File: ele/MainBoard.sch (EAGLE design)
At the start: 120 parts, among them IC1 MCP23017SP, IC2 74HC595D, IC3 74HC595D, X1 POWER_IN, X2 POWER_OUT

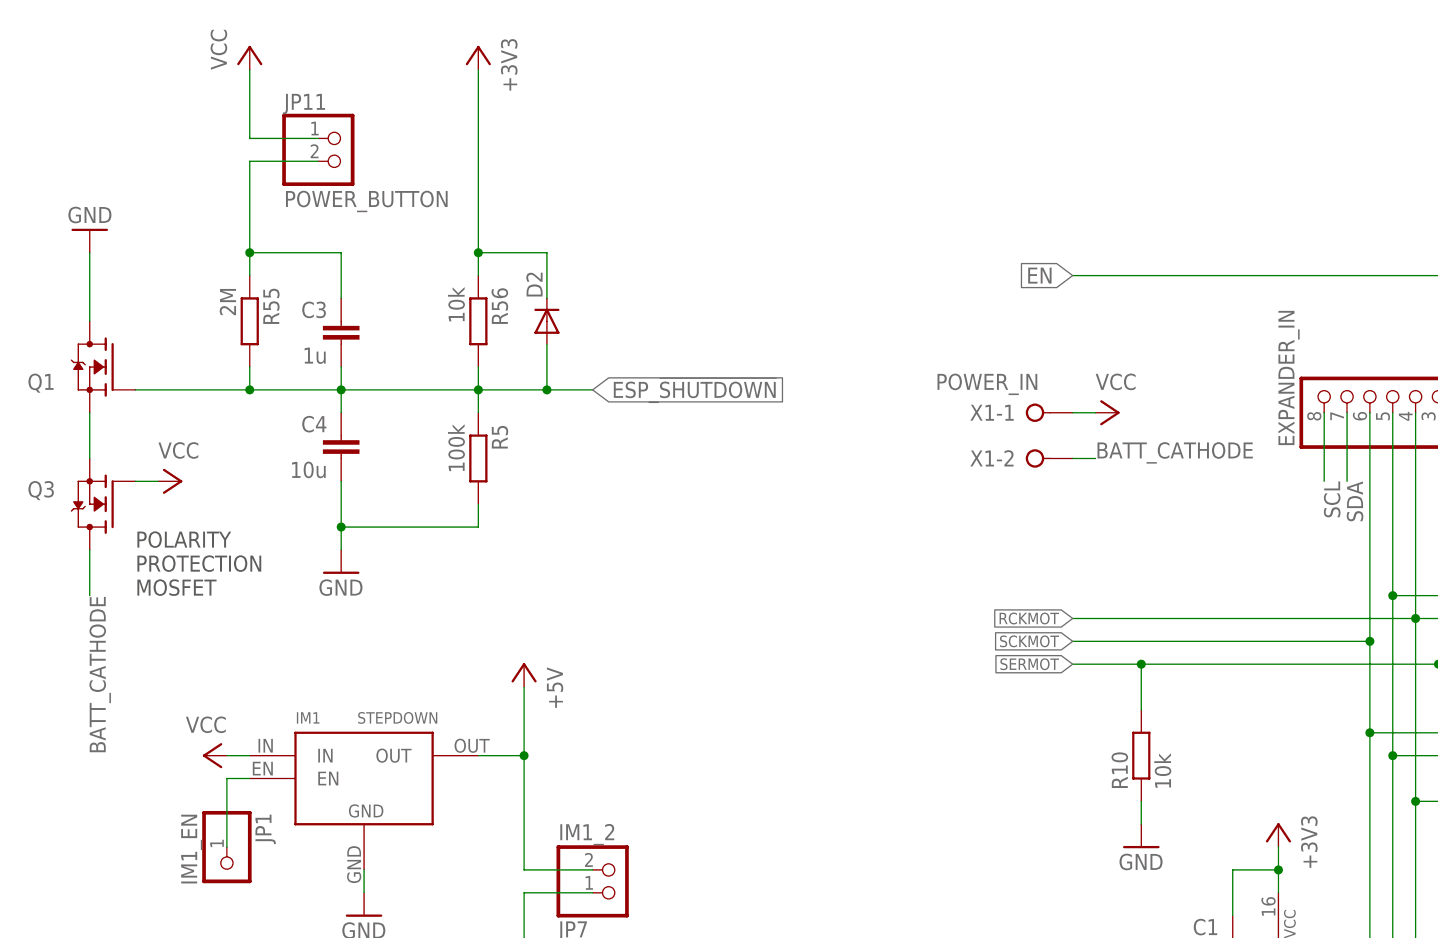
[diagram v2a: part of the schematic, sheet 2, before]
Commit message: ele: move power switch from GND to VCC (schematic only)
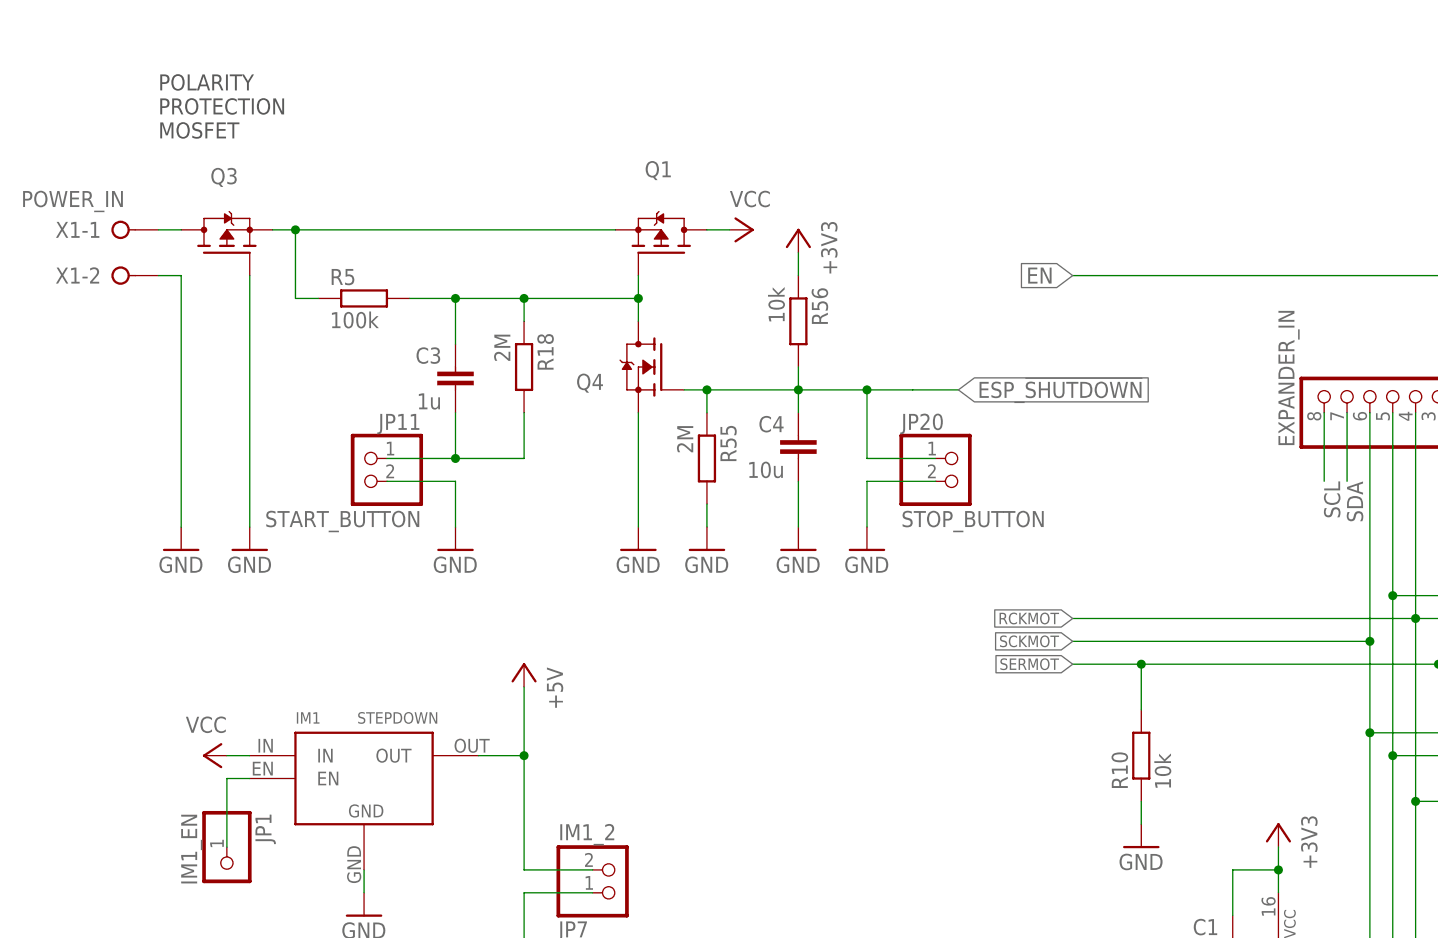
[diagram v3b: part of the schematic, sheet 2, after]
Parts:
- removed D2: (no value), diode:DIODE-SOD123
- added JP20: STOP_BUTTON, pinhead:PINHD-1X2
- added Q4: (no value), transistors:N-MOSFET-TO92
- added R18: 2M, rcl_upravena:R-EU_0204/2V
- JP11: value POWER_BUTTON -> START_BUTTON
- Q1, Q3: device transistors:N-MOSFET-TO220V -> transistors:P-MOSFET-TO220V
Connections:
- removed net BATT_CATHODE: Q3.D, X1-2.KL
- removed net BATT_CATHODE2: Q1.S, Q3.S
- removed net N$19: C3.1, JP11.2, R55.1
- new net BAT: Q3.D, X1-1.KL
- new net BAT_PROT: Q1.S, Q3.S, R5.1
- new net N$1: C3.1, Q1.G, Q4.D, R18.1, R5.2
- new net N$6: C3.2, JP11.1, R18.2
- net +3V3: no longer D2.C
- net ESP_!SHUTDOWN: now also JP20.1, Q4.G, R55.1; no longer C3.2, D2.A, Q1.G, R5.1, R55.2
- net GND: now also JP11.2, JP20.2, Q3.G, Q4.S, R55.2, X1-2.KL; no longer Q1.D, R5.2
- net VCC: now also Q1.D; no longer JP11.1, Q3.G, X1-1.KL
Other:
- moved on the sheet: C3, C4, JP11, Q1, Q3, R5, R55, R56, X1-1, X1-2

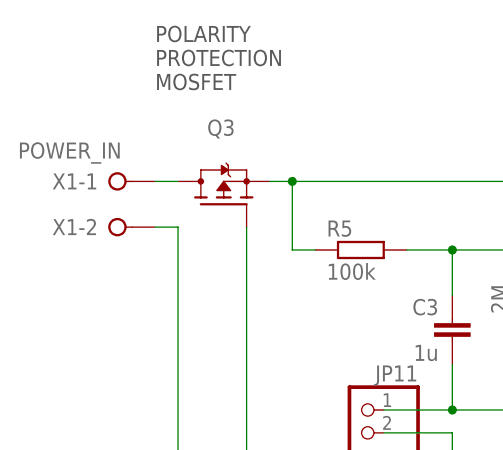
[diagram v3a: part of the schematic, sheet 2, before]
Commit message: ele: Fix layout on left side (motor drivers)
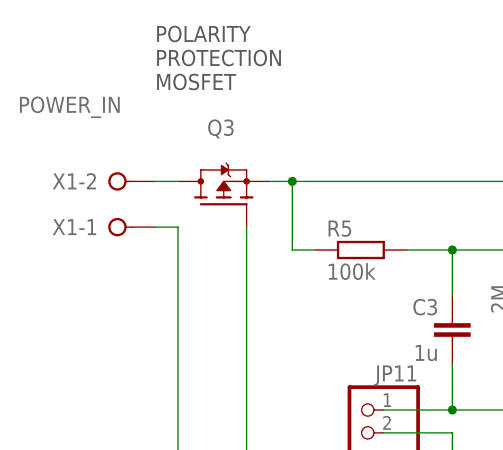
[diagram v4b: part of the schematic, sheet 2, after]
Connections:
- net BAT: now also X1-2.KL; no longer X1-1.KL
- net GND: now also X1-1.KL; no longer X1-2.KL
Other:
- moved on the sheet: X1-1, X1-2

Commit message: ele: MainBoard - join the start/stop pinheads
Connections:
- net N$1 renamed START_GATE
- net N$6 renamed START_BUTTON
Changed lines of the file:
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@@
 <?xml version="1.0" encoding="utf-8"?>
 <!DOCTYPE eagle SYSTEM "eagle.dtd">
-<eagle version="9.0.1">
+<eagle version="9.0.0">
 <drawing>
 <settings>
@@
 </segment>
 </net>
-<net name="N$1" class="0">
+<net name="START_GATE" class="0">
 <segment>
 <pinref part="R5" gate="G$1" pin="2"/>
@@
 </segment>
 </net>
-<net name="N$6" class="0">
+<net name="START_BUTTON" class="0">
 <segment>
 <pinref part="R18" gate="G$1" pin="2"/>

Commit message: ele: Added PIEZO to MainBoard.
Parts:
- added U$1: PIEZO, piezo:PIEZO
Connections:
- net ENC7A: now also U$1.+
- net ENC7B_: now also U$1.-
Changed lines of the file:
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@@
 <?xml version="1.0" encoding="utf-8"?>
 <!DOCTYPE eagle SYSTEM "eagle.dtd">
-<eagle version="9.0.0">
+<eagle version="9.0.1">
 <drawing>
 <settings>
@@
 <part name="JP20" library="pinhead" deviceset="PINHD-1X2" device="" value="STOP_BUTTON"/>
 <part name="GND52" library="supply1" library_urn="urn:adsk.eagle:library:371" deviceset="GND" device=""/>
+<part name="U$1" library="piezo" deviceset="PIEZO" device=""/>
 </parts>
 <sheets>
@@
 <instance part="GND14" gate="1" x="25.4" y="91.44"/>
 <instance part="P+27" gate="1" x="48.26" y="124.46"/>
+<instance part="U$1" gate="G$1" x="185.42" y="193.04" rot="R180"/>
 </instances>
 <busses>
@@
 <label x="205.74" y="187.96" size="1.778" layer="95" rot="R180"/>
 <pinref part="RN5" gate="B" pin="1"/>
-<wire x1="223.52" y1="187.96" x2="205.74" y2="187.96" width="0.1524" layer="91"/>
+<wire x1="223.52" y1="187.96" x2="190.5" y2="187.96" width="0.1524" layer="91"/>
+<pinref part="U$1" gate="G$1" pin="+"/>
 </segment>
 <segment>
@@
 <segment>
 <pinref part="RN5" gate="A" pin="2"/>
-<wire x1="248.92" y1="190.5" x2="233.68" y2="190.5" width="0.1524" layer="91"/>
+<wire x1="248.92" y1="190.5" x2="236.22" y2="190.5" width="0.1524" layer="91"/>
 <pinref part="IM6" gate="G$1" pin="IO33"/>
 <label x="238.76" y="190.5" size="1.778" layer="95"/>
+<wire x1="236.22" y1="190.5" x2="233.68" y2="190.5" width="0.1524" layer="91"/>
+<wire x1="236.22" y1="190.5" x2="236.22" y2="195.58" width="0.1524" layer="91"/>
+<wire x1="236.22" y1="195.58" x2="193.04" y2="195.58" width="0.1524" layer="91"/>
+<junction x="236.22" y="190.5"/>
+<pinref part="U$1" gate="G$1" pin="-"/>
+<wire x1="193.04" y1="195.58" x2="193.04" y2="190.5" width="0.1524" layer="91"/>
+<wire x1="193.04" y1="190.5" x2="190.5" y2="190.5" width="0.1524" layer="91"/>
 </segment>
 </net>

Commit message: ele: Modified tNames layer on the PCB design.
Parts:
- renumbered U$1 to PIEZO
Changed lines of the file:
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@@
 <part name="JP20" library="pinhead" deviceset="PINHD-1X2" device="" value="STOP_BUTTON"/>
 <part name="GND52" library="supply1" library_urn="urn:adsk.eagle:library:371" deviceset="GND" device=""/>
-<part name="U$1" library="piezo" deviceset="PIEZO" device=""/>
+<part name="PIEZO" library="piezo" deviceset="PIEZO" device=""/>
 </parts>
 <sheets>
@@
 <instance part="GND14" gate="1" x="25.4" y="91.44"/>
 <instance part="P+27" gate="1" x="48.26" y="124.46"/>
-<instance part="U$1" gate="G$1" x="185.42" y="193.04" rot="R180"/>
+<instance part="PIEZO" gate="G$1" x="185.42" y="193.04" rot="R180"/>
 </instances>
 <busses>
@@
 <pinref part="RN5" gate="B" pin="1"/>
 <wire x1="223.52" y1="187.96" x2="190.5" y2="187.96" width="0.1524" layer="91"/>
-<pinref part="U$1" gate="G$1" pin="+"/>
+<pinref part="PIEZO" gate="G$1" pin="+"/>
 </segment>
 <segment>
@@
 <wire x1="236.22" y1="195.58" x2="193.04" y2="195.58" width="0.1524" layer="91"/>
 <junction x="236.22" y="190.5"/>
-<pinref part="U$1" gate="G$1" pin="-"/>
+<pinref part="PIEZO" gate="G$1" pin="-"/>
 <wire x1="193.04" y1="195.58" x2="193.04" y2="190.5" width="0.1524" layer="91"/>
 <wire x1="193.04" y1="190.5" x2="190.5" y2="190.5" width="0.1524" layer="91"/>

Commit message: ele: MainBoard - move I2C pinheads to right due to USB cable for EPS32
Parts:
- removed JP43: I2C3_5V, pinhead:PINHD-1X4
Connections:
- net +5V: no longer JP43.4
- net GND: no longer JP43.3
- net SCL5V: no longer JP43.1
- net SDA5V: no longer JP43.2
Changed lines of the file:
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@@
 <?xml version="1.0" encoding="utf-8"?>
 <!DOCTYPE eagle SYSTEM "eagle.dtd">
-<eagle version="9.0.1">
+<eagle version="9.0.0">
 <drawing>
 <settings>
@@
 <part name="JP41" library="pinhead" library_urn="urn:adsk.eagle:library:325" deviceset="PINHD-1X4" device="" package3d_urn="urn:adsk.eagle:package:22407/2" value="I2C2_3V3"/>
 <part name="JP42" library="pinhead" library_urn="urn:adsk.eagle:library:325" deviceset="PINHD-1X4" device="" package3d_urn="urn:adsk.eagle:package:22407/2" value="I2C3_3V3"/>
-<part name="JP43" library="pinhead" library_urn="urn:adsk.eagle:library:325" deviceset="PINHD-1X4" device="" package3d_urn="urn:adsk.eagle:package:22407/2" value="I2C3_5V"/>
 <part name="JP44" library="pinhead" library_urn="urn:adsk.eagle:library:325" deviceset="PINHD-1X4" device="" package3d_urn="urn:adsk.eagle:package:22407/2" value="I2C2_5V"/>
 <part name="JP45" library="pinhead" library_urn="urn:adsk.eagle:library:325" deviceset="PINHD-1X4" device="" package3d_urn="urn:adsk.eagle:package:22407/2" value="I2C1_5V"/>
@@
 <instance part="JP41" gate="A" x="73.66" y="50.8"/>
 <instance part="JP42" gate="A" x="86.36" y="50.8"/>
-<instance part="JP43" gate="A" x="86.36" y="30.48"/>
 <instance part="JP44" gate="A" x="73.66" y="30.48"/>
 <instance part="JP45" gate="A" x="60.96" y="30.48"/>
@@
 <wire x1="58.42" y1="30.48" x2="71.12" y2="30.48" width="0.1524" layer="91"/>
 <junction x="58.42" y="30.48"/>
-<pinref part="JP43" gate="A" pin="3"/>
 <wire x1="71.12" y1="30.48" x2="83.82" y2="30.48" width="0.1524" layer="91"/>
 <junction x="71.12" y="30.48"/>
@@
 <wire x1="58.42" y1="27.94" x2="71.12" y2="27.94" width="0.1524" layer="91"/>
 <junction x="58.42" y="27.94"/>
-<pinref part="JP43" gate="A" pin="4"/>
 <wire x1="71.12" y1="27.94" x2="83.82" y2="27.94" width="0.1524" layer="91"/>
 <junction x="71.12" y="27.94"/>
@@
 <wire x1="58.42" y1="33.02" x2="71.12" y2="33.02" width="0.1524" layer="91"/>
 <junction x="58.42" y="33.02"/>
-<pinref part="JP43" gate="A" pin="2"/>
 <wire x1="71.12" y1="33.02" x2="83.82" y2="33.02" width="0.1524" layer="91"/>
 <junction x="71.12" y="33.02"/>
@@
 <wire x1="58.42" y1="35.56" x2="71.12" y2="35.56" width="0.1524" layer="91"/>
 <junction x="58.42" y="35.56"/>
-<pinref part="JP43" gate="A" pin="1"/>
 <wire x1="71.12" y1="35.56" x2="83.82" y2="35.56" width="0.1524" layer="91"/>
 <junction x="71.12" y="35.56"/>
